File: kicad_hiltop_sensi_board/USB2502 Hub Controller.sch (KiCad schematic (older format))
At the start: 39 parts, among them U27 USB2502, U7 AT24C02C-SSHM-T, Y1 50ppm 24.000MHZ

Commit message: Sensi board with references visible and without stitching vias
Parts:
- C101, C94, C95, C96, C97, C98, C99: value 0.1uf -> 0.1uF
- R109: Devtank 101-050 -> 101-044
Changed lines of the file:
@@
 P 8000 7200
 F 0 "C101" H 8115 7246 50  0000 L CNN
-F 1 "0.1uf" H 8115 7155 50  0000 L CNN
+F 1 "0.1uF" H 8115 7155 50  0000 L CNN
 F 2 "Capacitor_SMD:C_0402_1005Metric" H 8038 7050 50  0001 C CNN
 F 3 "" H 8000 7200 50  0001 C CNN
@@
 P 7600 7200
 F 0 "C96" H 7715 7246 50  0000 L CNN
-F 1 "0.1uf" H 7715 7155 50  0000 L CNN
+F 1 "0.1uF" H 7715 7155 50  0000 L CNN
 F 2 "Capacitor_SMD:C_0402_1005Metric" H 7638 7050 50  0001 C CNN
 F 3 "" H 7600 7200 50  0001 C CNN
@@
 P 7600 7650
 F 0 "C97" H 7715 7696 50  0000 L CNN
-F 1 "0.1uf" H 7715 7605 50  0000 L CNN
+F 1 "0.1uF" H 7715 7605 50  0000 L CNN
 F 2 "Capacitor_SMD:C_0402_1005Metric" H 7638 7500 50  0001 C CNN
 F 3 "" H 7600 7650 50  0001 C CNN
@@
 P 7600 6750
 F 0 "C95" H 7715 6796 50  0000 L CNN
-F 1 "0.1uf" H 7715 6705 50  0000 L CNN
+F 1 "0.1uF" H 7715 6705 50  0000 L CNN
 F 2 "Capacitor_SMD:C_0402_1005Metric" H 7638 6600 50  0001 C CNN
 F 3 "" H 7600 6750 50  0001 C CNN
@@
 P 8000 6250
 F 0 "C99" H 8115 6296 50  0000 L CNN
-F 1 "0.1uf" H 8115 6205 50  0000 L CNN
+F 1 "0.1uF" H 8115 6205 50  0000 L CNN
 F 2 "Capacitor_SMD:C_0402_1005Metric" H 8038 6100 50  0001 C CNN
 F 3 "" H 8000 6250 50  0001 C CNN
@@
 P 7600 6250
 F 0 "C94" H 7715 6296 50  0000 L CNN
-F 1 "0.1uf" H 7715 6205 50  0000 L CNN
+F 1 "0.1uF" H 7715 6205 50  0000 L CNN
 F 2 "Capacitor_SMD:C_0402_1005Metric" H 7638 6100 50  0001 C CNN
 F 3 "" H 7600 6250 50  0001 C CNN
@@
 F 3 "" H 7650 5850 50  0001 C CNN
 F 4 "1%" V 7650 5850 50  0001 C CNN "Tolerance"
-F 5 "101-050" H 7650 5850 50  0001 C CNN "Devtank"
+F 5 "101-044" H 7650 5850 50  0001 C CNN "Devtank"
 	1    7650 5850
 	0    -1   -1   0
@@
 P 7600 8100
 F 0 "C98" H 7715 8146 50  0000 L CNN
-F 1 "0.1uf" H 7715 8055 50  0000 L CNN
+F 1 "0.1uF" H 7715 8055 50  0000 L CNN
 F 2 "Capacitor_SMD:C_0402_1005Metric" H 7638 7950 50  0001 C CNN
 F 3 "" H 7600 8100 50  0001 C CNN

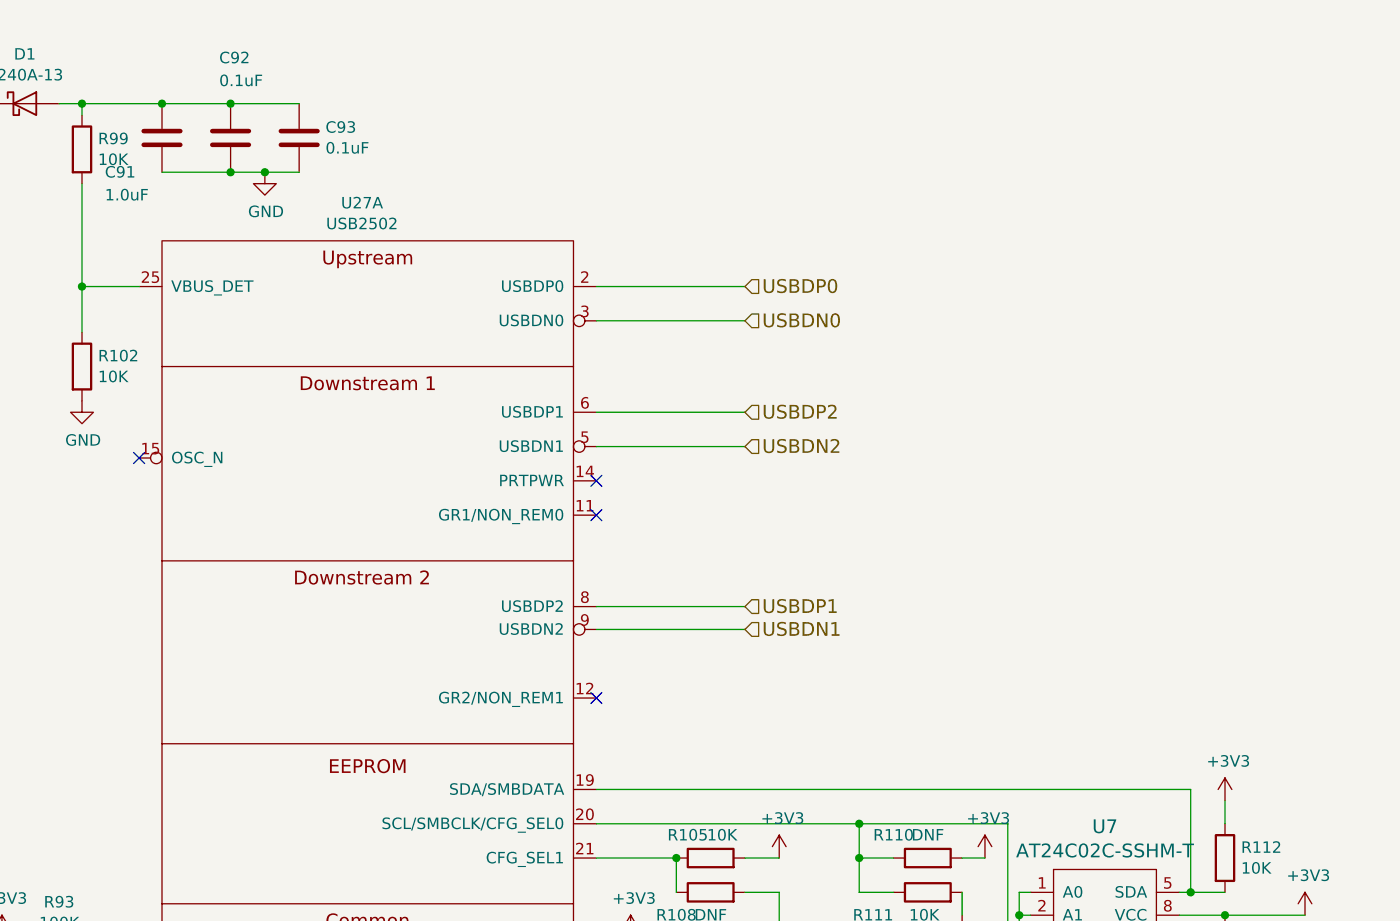
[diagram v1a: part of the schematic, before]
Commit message: Changes to Sensi board after review
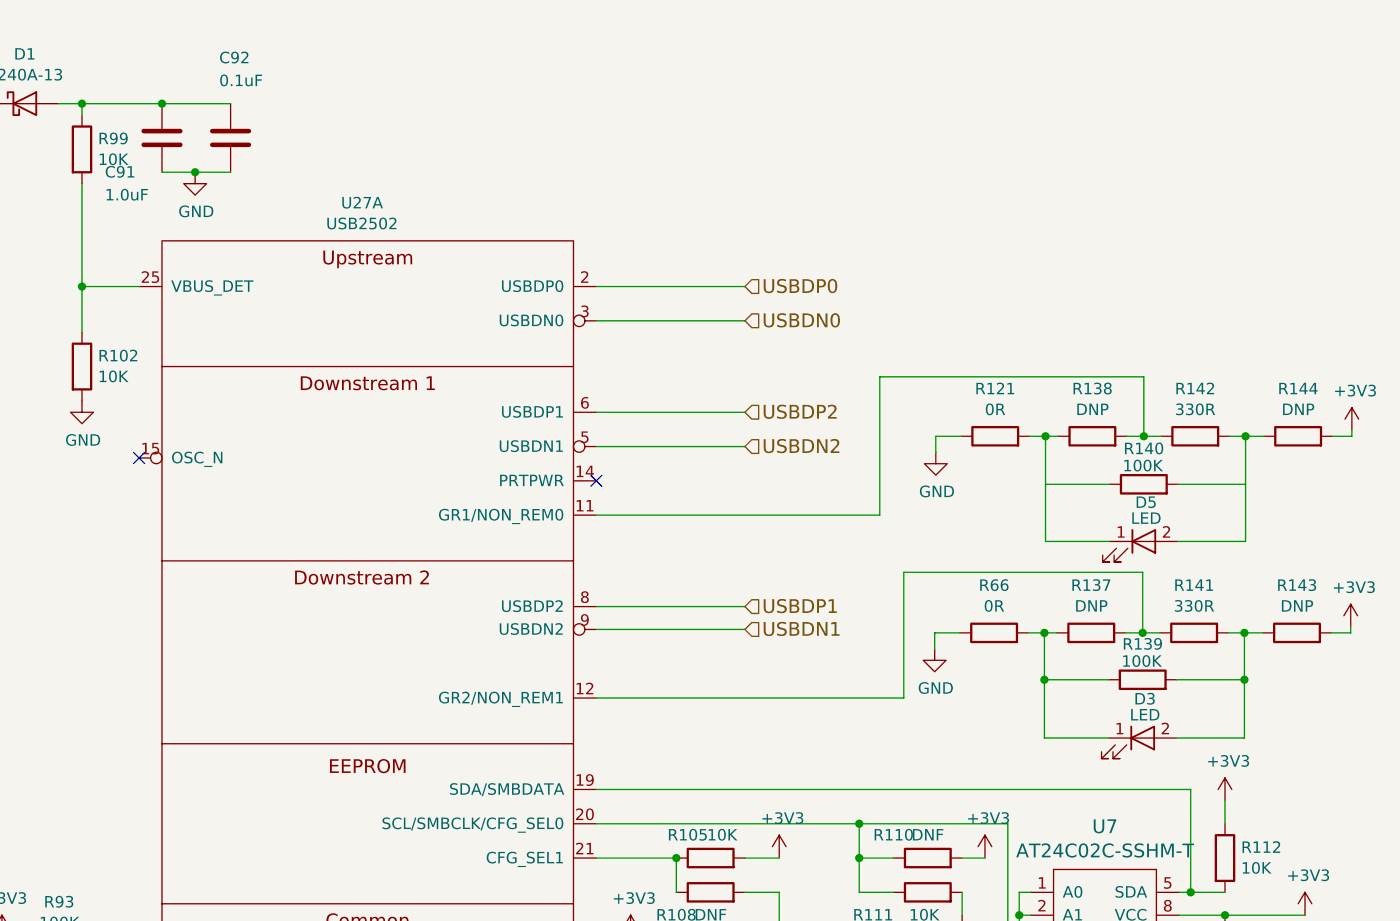
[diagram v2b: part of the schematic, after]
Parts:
- removed C93: 0.1uF, Capacitor_SMD:C_0402_1005Metric, symbol device:C
- added D3, D5: LED, symbol device:LED
- added R121, R66: 0R, symbol device:R
- added R137, R138, R143, R144: DNP, symbol device:R
- added R139, R140: 100K, symbol device:R
- added R141, R142: 330R, symbol device:R
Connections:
- net +3V3: now also R143.2, R144.2
- net GND: now also R121.1, R66.1
- net at U27.11 (GR1/NON_REM0): now also R138.2, R142.1
- net at U27.12 (GR2/NON_REM1): now also R137.2, R141.1
- new net: D3.2 (A), R139.2, R141.2, R143.1
- new net: D3.1 (K), R137.1, R139.1, R66.2
- new net: D5.2 (A), R142.2, R144.1
- new net: D5.1 (K), R121.2, R138.1
- no-connect marks 5 -> 3
